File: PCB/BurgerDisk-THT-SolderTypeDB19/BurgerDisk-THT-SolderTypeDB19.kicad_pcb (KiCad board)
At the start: 2 copper layers, 93.7 x 67.6 mm, 18 parts, among them J1 Daisy port in, J2 MicroSD module, J3 UART, J4 Daisy port out, U1 PC817

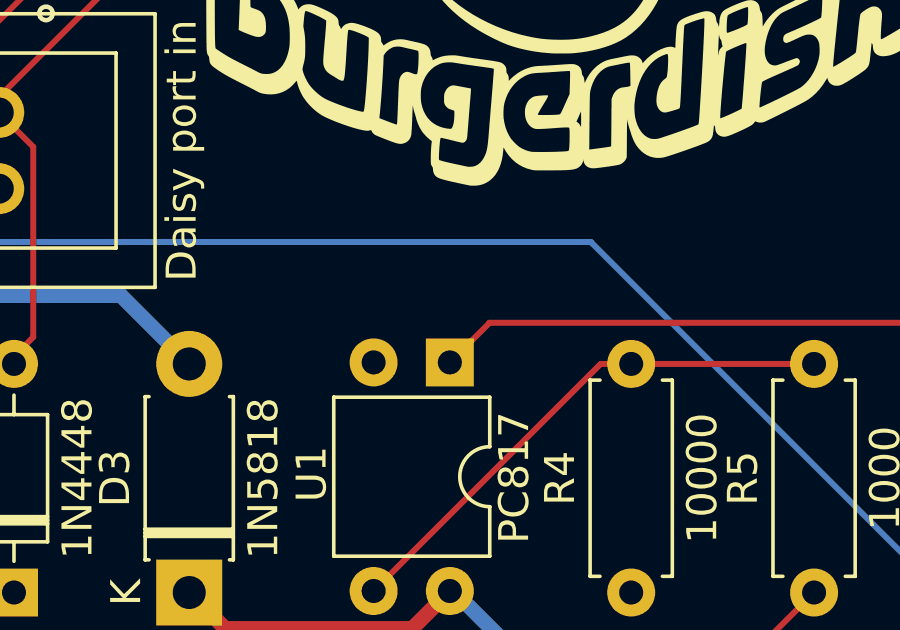
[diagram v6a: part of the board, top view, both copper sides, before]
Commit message: Add indicator on PC817 pin1
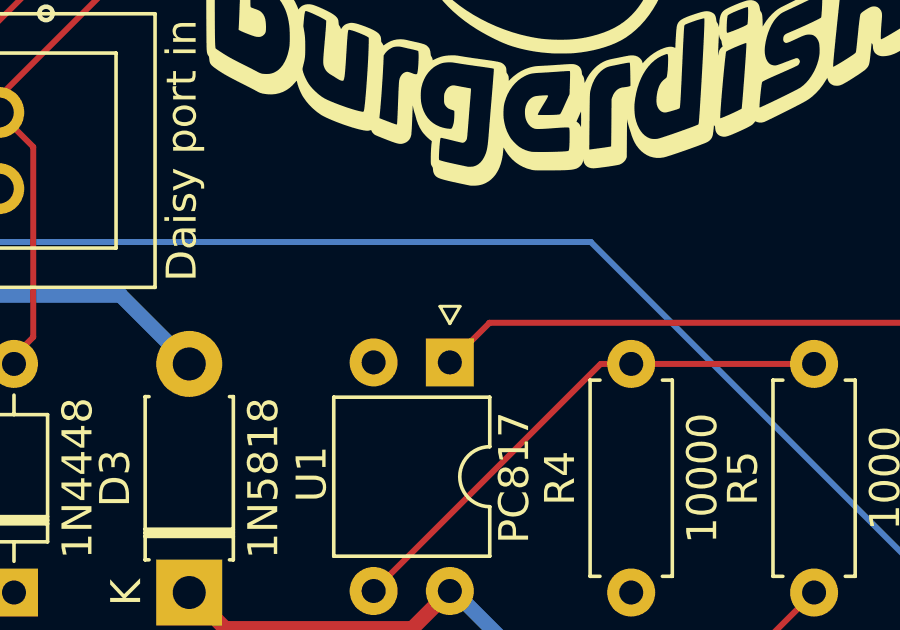
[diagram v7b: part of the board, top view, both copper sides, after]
